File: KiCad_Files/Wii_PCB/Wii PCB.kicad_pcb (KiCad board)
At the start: 4 copper layers, 62.2 x 71.5 mm, 203 parts, among them J1 Conn_01x20_Pin, U5 27M, Y1 ABS06-107-32.768KHZ-T

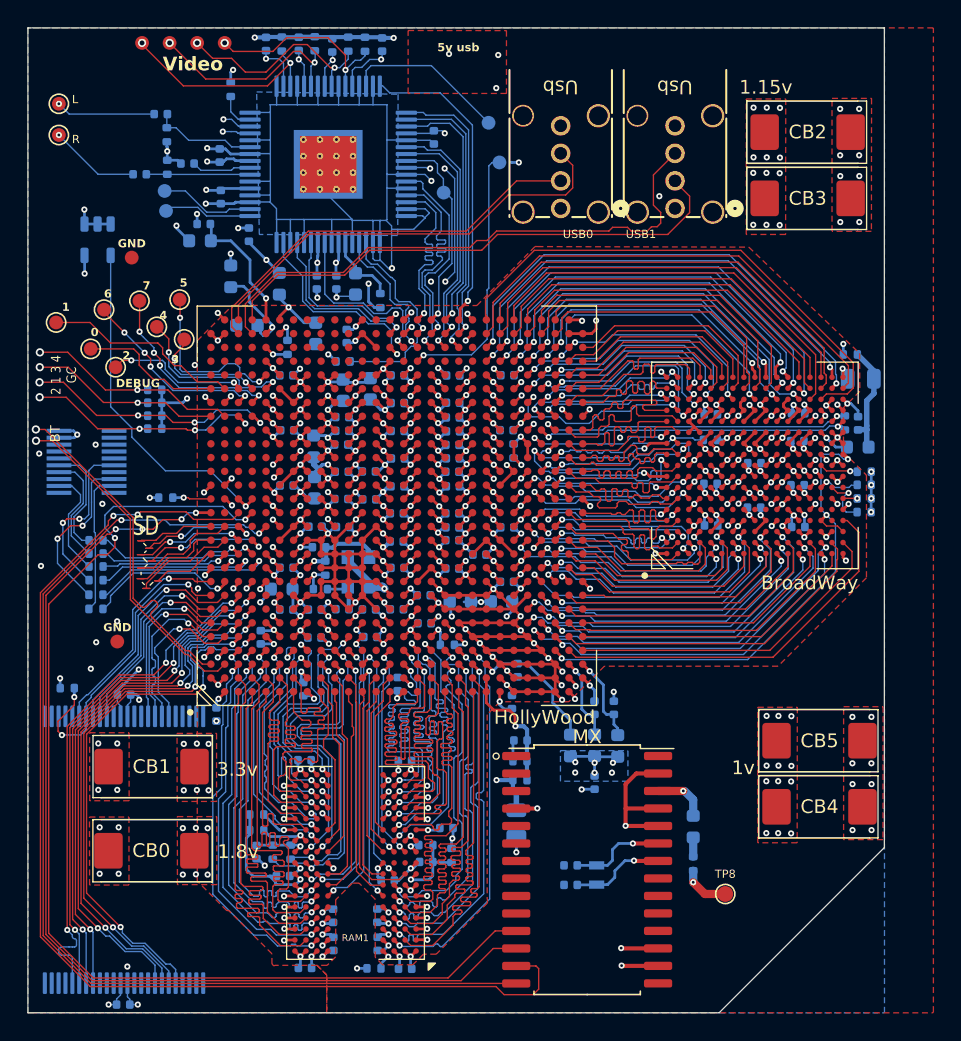
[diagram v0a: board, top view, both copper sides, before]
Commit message: Updated RAM & GPU bus to allow custom net rules for measuring intra-track spacing, added pad for reset, removed debug pads, reorganized ram schematic to cluster length matched signals, changed MX chip and U10 symbols, and re-labeled the wifi net interface.
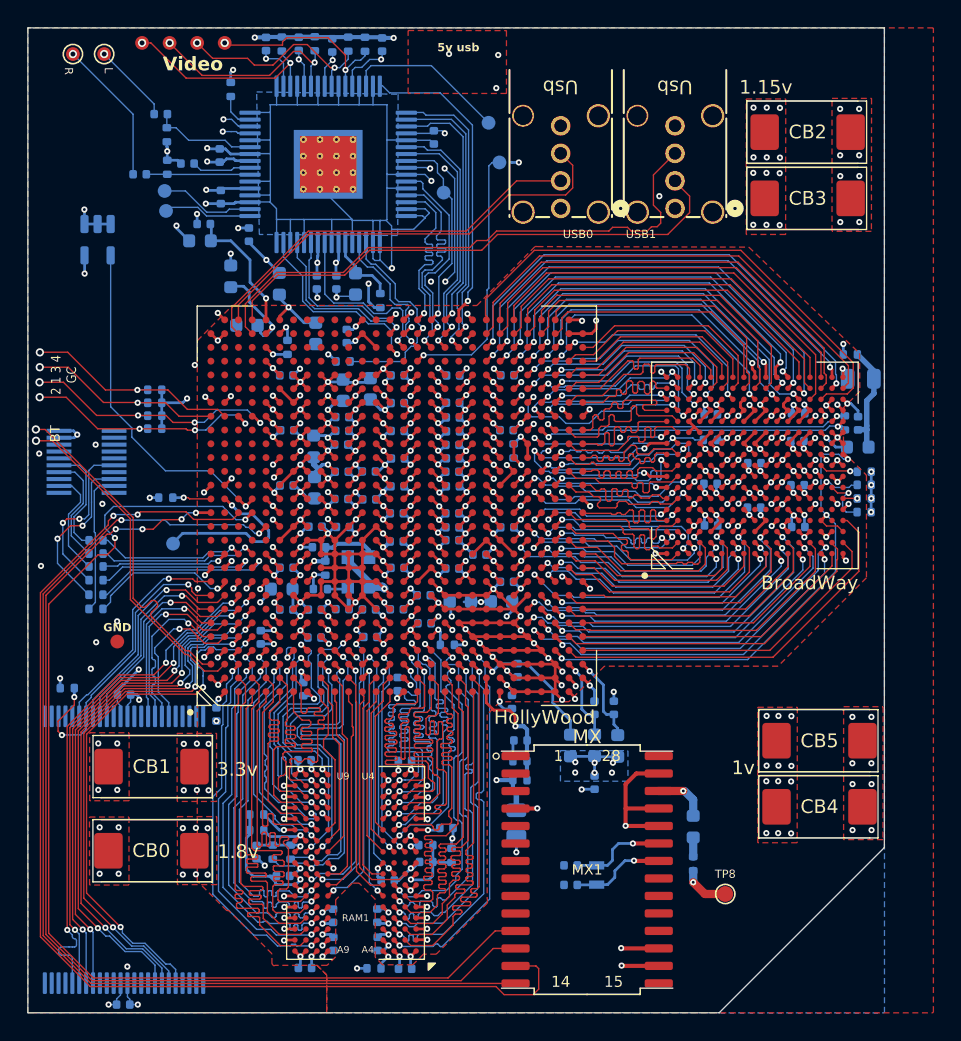
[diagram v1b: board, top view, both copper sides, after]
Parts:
- removed the ? at (109.8, 64.6)
- removed TP0, TP1, TP2, TP3, TP4, TP5, TP6, TP7: TestPoint, TestPoint:TestPoint_Pad_D1.0mm
- added RESET1: TestPoint, TestPoint:TestPoint_Pad_D1.0mm, B.Cu at (112.8, 85.4)
- BROADWAY1: footprint wii_bgaLibrary:Updated BROADWAY -> WeeWii_Library:Updated BROADWAY
- HOLLYWOOD1: footprint wii_bgaLibrary:Updated HOLLYWOOD -> WeeWii_Library:Updated HOLLYWOOD
- J1: footprint Connector_Molex:Molex_SlimStack_52991-0208_2x10_P0.50mm_Vertical -> WeeWii_Library:Molex_SlimStack_Wifi
- MX1: renamed from U2; footprint wii_bgaLibrary:MX_SOIC -> WeeWii_Library:MX_SOIC
- RAM1: footprint wii_bgaLibrary:GDDR3 -> WeeWii_Library:Updated GDDR3
- U10: value ~ -> BD45302G; footprint Package_TO_SOT_SMD:SOT-23-5 -> WeeWii_Library:u10
- Y1: footprint wii_bgaLibrary:Crystal_SMD_2012-2Pin_2.0x1.2mm -> WeeWii_Library:Crystal_SMD_2012-2Pin_2.0x1.2mm
- moved TPR1 5.97 mm to (105.5, 49.8), turned to -90 degrees
- moved TPL1 4.88 mm to (107.8, 49.8), turned to -90 degrees
- moved RAM1 2.43 mm to (126.0, 108.5)
- renumbered U1 to AVE1
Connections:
- net CPUAACKB renamed GPU_CPUAACKB
- net CPUCLK renamed GPU_CPUCLK
- net CPUCLKB renamed GPU_CPUCLKB
- net CPUINTB renamed GPU_CPUINTB
- net CPURSTB renamed GPU_CPURSTB
- net CPUSRSTB renamed GPU_CPUSRSTB
- net CPUTAB renamed GPU_CPUTAB
- net CPUTBSTB renamed GPU_CPUTBSTB
- net CPUTSB renamed GPU_CPUTSB
- net CPUTSIZ0 renamed GPU_CPUTSIZ0
- net CPUTSIZ1 renamed GPU_CPUTSIZ1
- net CPUTSIZ2 renamed GPU_CPUTSIZ2
- net CPUTT0 renamed GPU_CPUTT0
- net CPUTT1 renamed GPU_CPUTT1
- net CPUTT2 renamed GPU_CPUTT2
- net CPUTT3 renamed GPU_CPUTT3
- net CPUTT4 renamed GPU_CPUTT4
- net DISC_DRIVE0 renamed DID7
- net DISC_DRIVE1 renamed DID6
- net DISC_DRIVE10 renamed DIBRK
- net DISC_DRIVE11 renamed DICOVER
- net DISC_DRIVE12 renamed ~{DIRST}
- net DISC_DRIVE13 renamed DID1
- net DISC_DRIVE14 renamed DID0
- net DISC_DRIVE15 renamed DIDIR
- net DISC_DRIVE16 renamed ~{DIHSTR}
- net DISC_DRIVE17 renamed ~{DIDSTR}
- net DISC_DRIVE18 renamed NOSPINUP
- net DISC_DRIVE2 renamed AISCLK
- net DISC_DRIVE3 renamed AISD
- net DISC_DRIVE4 renamed DID5
- net DISC_DRIVE5 renamed DID4
- net DISC_DRIVE6 renamed AISLR
- net DISC_DRIVE7 renamed ~{DIERR}
- net DISC_DRIVE8 renamed DID3
- net DISC_DRIVE9 renamed DID2
- net GC_CARD_P1 renamed A_SEN
- net GC_CARD_P11 renamed A_CLK
- net GC_CARD_P13 renamed B_SEN
- net GC_CARD_P15 renamed B_INT
- net GC_CARD_P17 renamed B_DIN
- net GC_CARD_P19 renamed B_DOUT
- net GC_CARD_P21 renamed B_CS
- net GC_CARD_P23 renamed B_CLK
- net GC_CARD_P3 renamed A_INT
- net GC_CARD_P5 renamed A_DIN
- net GC_CARD_P7 renamed A_DOUT
- net GC_CARD_P9 renamed A_CS
- net PIN16 renamed WIFI_SDIO3
- net PIN17 renamed WIFI_SDIO0
- net PIN19 renamed WIFI_SDIOCMD
- net PIN2 renamed WIFI_SDIO2
- net PIN3 renamed WIFI_SDIO1
- net PIN5 renamed WIFI_SDIOCLK
- net mx_pin11 renamed GPU_EXI0_DO
- net mx_pin12 renamed GPU_EXI0_DI
- net mx_pin13 renamed GPU_EXI0_~{CS}
- net mx_pin14 renamed GPU_EXI0_CLK
- net mx_pin24 renamed Delay_Enable
- net sd_data1 renamed SD_CMD
- net sd_data2 renamed SD_DAT3
- net sd_data3 renamed SD_DAT2
- net sd_data4 renamed SD_CLK
- net sd_data5 renamed SD_WP
- net sd_data6 renamed SD_CD
- net sd_data7 renamed SD_DAT1
- net sd_data8 renamed SD_DAT0
- HOLLYWOOD1 pad A3: BT -> ~{BT}
- HOLLYWOOD1 pad B3: ~{BT} -> BT
- HOLLYWOOD1 pad D1: WDQS1 -> RAM_WDQS1
- HOLLYWOOD1 pad D3: RDQS1 -> RAM_RDQS1
- HOLLYWOOD1 pad D4: DM1 -> RAM_DM1
- HOLLYWOOD1 pad F2: WDQS2 -> RAM_WDQS2
- HOLLYWOOD1 pad G3: DM2 -> RAM_DM2
- HOLLYWOOD1 pad G4: RDQS2 -> RAM_RDQS2
- HOLLYWOOD1 pad K2: WE# -> RAM_WE#
- HOLLYWOOD1 pad K3: CK# -> RAM_CK0#
- HOLLYWOOD1 pad K4: CK -> RAM_CK0
- HOLLYWOOD1 pad L1: BA1 -> RAM_BA1
- HOLLYWOOD1 pad L2: BA0 -> RAM_BA0
- HOLLYWOOD1 pad L4: BA2 -> RAM_BA2
- HOLLYWOOD1 pad L5: RES -> RAM_RES
- HOLLYWOOD1 pad M2: CAS# -> RAM_CAS#
- HOLLYWOOD1 pad M3: RAS# -> RAM_RAS#
- HOLLYWOOD1 pad M5: CS# -> RAM_CS0#
- HOLLYWOOD1 pad N2: CKE -> RAM_CKE
- HOLLYWOOD1 pad T3: RDQS3 -> RAM_RDQS3
- HOLLYWOOD1 pad T4: DM3 -> RAM_DM3
- HOLLYWOOD1 pad U1: WDQS3 -> RAM_WDQS3
- HOLLYWOOD1 pad W2: WDQS0 -> RAM_WDQS0
- HOLLYWOOD1 pad W3: DM0 -> RAM_DM0
- HOLLYWOOD1 pad W4: RDQS0 -> RAM_RDQS0
- J1 pad 10: W_R16 -> unconnected-(J1-Pin_10-Pad10)
- J1 pad 11: GND -> 3.3V
- J1 pad 12: GND -> 3.3V
- J1 pad 13: unconnected-(J1-Pin_13-Pad13) -> GND
- J1 pad 16: GND -> R_WIFI_SDIO3
- J1 pad 17: unconnected-(J1-Pin_17-Pad17) -> R_WIFI_SDIO0
- J1 pad 18: 3.3V -> GND
- J1 pad 19: unconnected-(J1-Pin_19-Pad19) -> R_WIFI_SDIOCMD
- J1 pad 2: GND -> R_WIFI_SDIO2
- J1 pad 20: 3.3V -> GND
- J1 pad 3: W_R2 -> R_WIFI_SDIO1
- J1 pad 4: W_R19 -> GND
- J1 pad 5: W_R3 -> R_WIFI_SDIOCLK
- J1 pad 7: GND -> unconnected-(J1-Pin_7-Pad7)
- J1 pad 8: W_R17 -> GND
- J1 pad 9: W_R5 -> unconnected-(J1-Pin_9-Pad9)
- R11 pad 2: CK -> RAM_CK0
- R12 pad 2: CK# -> RAM_CK0#
- R212 pad 1: W_R2 -> R_WIFI_SDIO2
- R213 pad 1: W_R3 -> R_WIFI_SDIO1
- R8 pad 2: ZQ -> RAM_ZQ
- RA20_1 pad 1: W_R5 -> R_WIFI_SDIOCLK
- RA20_2 pad 1: W_R19 -> R_WIFI_SDIOCMD
- RA20_3 pad 1: W_R17 -> R_WIFI_SDIO0
- RA20_4 pad 1: W_R16 -> R_WIFI_SDIO3
- RAM1 pad A2: GND -> 1.8V
- RAM1 pad A3: RES -> GND
- RAM1 pad A4: GND -> RAM_ZQ
- RAM1 pad B1: RAM_DQ22 -> GND
- RAM1 pad B2: RAM_DQ23 -> RAM_DQ0
- RAM1 pad B3: GND -> RAM_DQ1
- RAM1 pad C1: RAM_DQ20 -> 1.8V
- RAM1 pad C2: RAM_DQ21 -> RAM_DQ2
- RAM1 pad C3: 1.8V -> RAM_DQ3
- RAM1 pad D1: WDQS2 -> GND
- RAM1 pad D2: RDQS2 -> RAM_WDQS0
- RAM1 pad D3: GND -> RAM_RDQS0
- RAM1 pad E1: RAM_DQ18 -> 1.8V
- RAM1 pad E2: DM2 -> RAM_DQ4
- RAM1 pad E3: 1.8V -> RAM_DM0
- RAM1 pad F1: RAM_DQ16 -> 1.8V
- RAM1 pad F2: RAM_DQ19 -> RAM_DQ6
- RAM1 pad F3: RAM_A9 -> RAM_DQ5
- RAM1 pad F4: RAM_A3 -> RAM_CAS#
- RAM1 pad G2: RAM_DQ17 -> GND
- RAM1 pad G3: RAM_A7 -> RAM_DQ7
- RAM1 pad G4: RAM_A11 -> RAM_BA0
- RAM1 pad H1: RAM_A8 -> ram_vref1
- RAM1 pad H2: RAM_A6 -> RAM_A1
- RAM1 pad H3: RAM_A4 -> RAM_RAS#
- RAM1 pad H4: RAM_A0 -> RAM_CKE
- RAM1 pad J1: RAM_A5 -> GND
- RAM1 pad J2: BA2 -> unconnected-(RAM1B-NC-PadJ2)
- RAM1 pad J3: WE# -> unconnected-(RAM1B-NC-PadJ3)
- RAM1 pad J4: CKE -> 1.8V
- RAM1 pad K1: GND -> 1.8V
- RAM1 pad K2: RAM_DQ15 -> RAM_A10
- RAM1 pad K3: BA1 -> RAM_A2
- RAM1 pad K4: BA0 -> RAM_A0
- RAM1 pad L1: RAM_DQ14 -> GND
- RAM1 pad L2: RAM_DQ13 -> GND
- RAM1 pad L3: CS# -> RAM_DQ25
- RAM1 pad L4: CAS# -> RAM_A11
- RAM1 pad M1: RAM_DQ12 -> 1.8V
- RAM1 pad M2: DM1 -> RAM_DQ24
- RAM1 pad M3: 1.8V -> RAM_DQ27
- RAM1 pad M4: 1.8V -> RAM_A3
- RAM1 pad N1: WDQS1 -> 1.8V
- RAM1 pad N2: RDQS1 -> RAM_DQ26
- RAM1 pad N3: GND -> RAM_DM3
- RAM1 pad N4: GND -> 1.8V
- RAM1 pad P1: RAM_DQ8 -> GND
- RAM1 pad P2: RAM_DQ9 -> RAM_WDQS3
- RAM1 pad P3: GND -> RAM_RDQS3
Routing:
- net RAM_CK0: track 0.00 -> 27.8 mm, vias 0 -> 2
- net CK: track 27.8 -> 0.00 mm, vias 2 -> 0
- net RAM_DM1: track 0.00 -> 27.0 mm, vias 0 -> 2
- net DM1: track 27.0 -> 0.00 mm, vias 2 -> 0
- net RDQS1: track 26.6 -> 0.00 mm, vias 2 -> 0
- net RAM_RDQS1: track 0.00 -> 26.6 mm, vias 0 -> 2
- net RAM_DM0: track 0.00 -> 26.3 mm, vias 0 -> 2
- net DM0: track 26.3 -> 0.00 mm, vias 2 -> 0
- net RDQS0: track 26.0 -> 0.00 mm, vias 2 -> 0
- net RAM_RDQS0: track 0.00 -> 26.0 mm, vias 0 -> 2
- net WDQS0: track 25.9 -> 0.00 mm
- net RAM_WDQS0: track 0.00 -> 25.9 mm
- net WDQS1: track 25.9 -> 0.00 mm
- net RAM_WDQS1: track 0.00 -> 25.9 mm
- net RAM_CK0#: track 0.00 -> 24.5 mm, vias 0 -> 2
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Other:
- board text removed: "0"
- board text removed: "1"
- board text removed: "2"
- board text removed: "3"
- board text removed: "4"
- board text removed: "5"
- board text removed: "6"
- board text removed: "7"
- board text removed: "AVE"
- board text removed: "DEBUG"
- board text removed: "SD"
- board text removed: "U10"
